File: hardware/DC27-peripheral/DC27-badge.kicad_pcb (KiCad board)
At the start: 2 copper layers, 106 parts, among them J1 Conn_01x02_Male, J2 USB_MICRO_RIGHT, J3 AudioJack3_Ground, J5 Conn_02x20_Odd_Even, J6 Conn_02x02_Counter_Clockwise, J7 Conn_ARM_JTAG_SWD_10, SW1 UP, SW2 DN, SW3 LEFT, SW4 RIGHT, SW5 A, SW6 B, SW7 RESET, U1 BMD-340-A-R, U2 IS31FL736, U3 MIC2288, U4 MCP73811T-435I-OT, U5 PAM2305AAB120, U6 MAX17043, U7 CS4344-CZZ, U8 TPD3E001DRLR

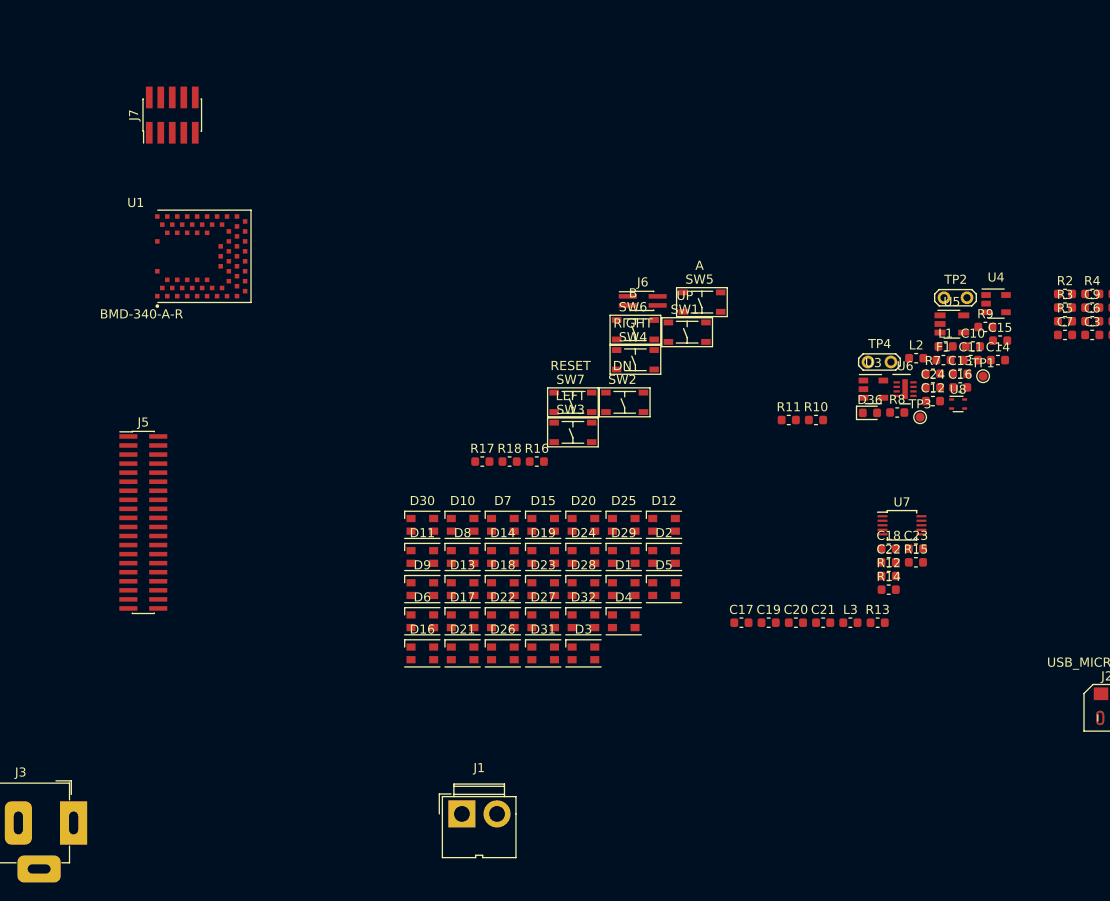
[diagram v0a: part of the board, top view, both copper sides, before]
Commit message: Update the main schematic with pins from bill's changes
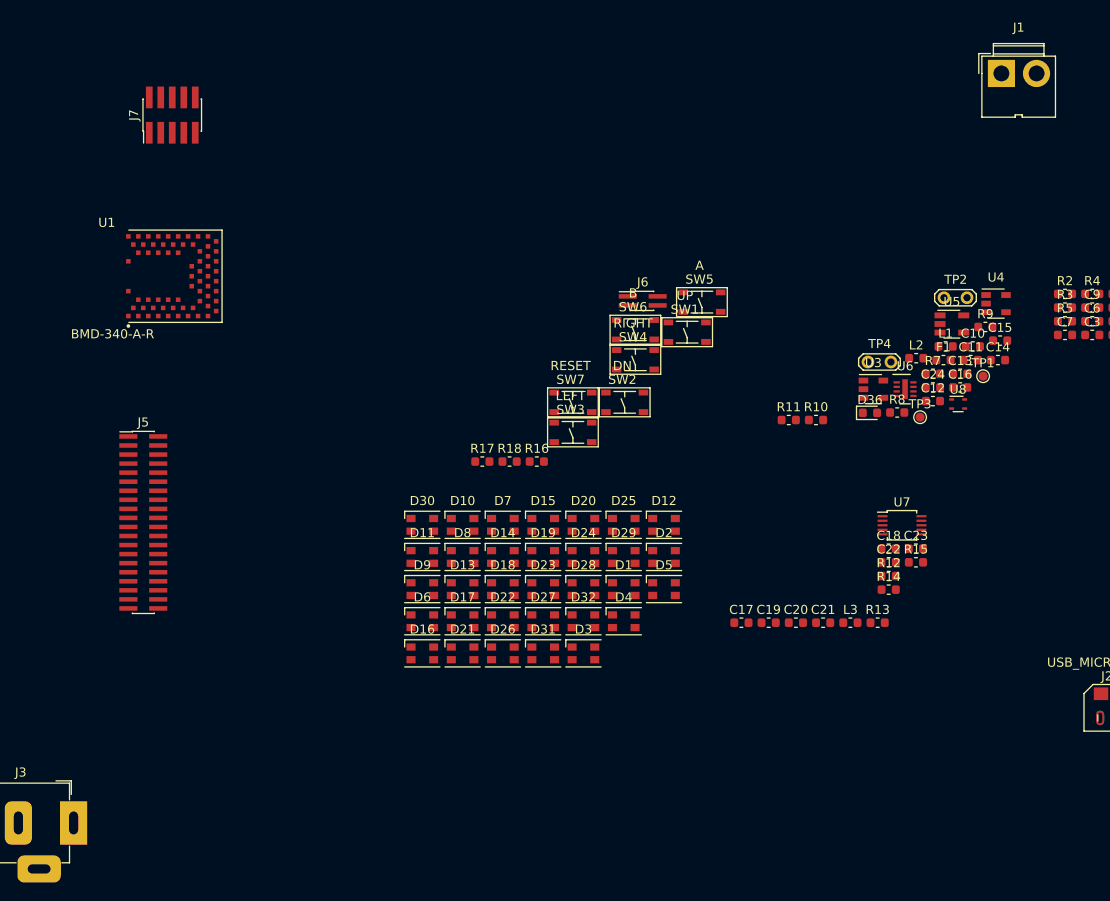
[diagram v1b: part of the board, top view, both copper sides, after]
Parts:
- moved J1 101.2 mm to (164.6, 30.8)
- moved U1 3.88 mm to (71.0, 53.2)
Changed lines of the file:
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@@
   )
   (module BMD-340-A-R:RIGADO_BMD-340-A-R (layer F.Cu)
-    (at 74.2 51)
+    (at 71 53.2)
     (attr smd)
     (fp_text reference U1 (at -5.23628 -5.9147) (layer F.SilkS)
@@
   )
   (module Connector:JWT_A3963_1x02_P3.96mm_Vertical (layer F.Cu)
-    (at 105 112.6)
+    (at 164.6 30.8)
     (descr "JWT A3963, 3.96mm pitch Pin head connector (http://www.jwt.com.tw/pro_pdf/A3963.pdf)")
     (tags "connector JWT A3963 pinhead")

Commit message: checkpoint everything - schematic passing DRC
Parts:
- removed C1, C3, C5, C7: 0.47uF, Capacitor_SMD:C_0603_1608Metric
- removed C10, C12, C13: 4.7uF, Capacitor_SMD:C_0603_1608Metric
- removed C11, C15: 22uF, Capacitor_SMD:C_0603_1608Metric
- removed C14, C23: 10uF, Capacitor_SMD:C_0603_1608Metric
- removed C16: 1.0uF, Capacitor_SMD:C_0603_1608Metric
- removed C17, C18, C19, C2, C24, C4, C6, C8: 0.1uF, Capacitor_SMD:C_0603_1608Metric
- removed C20, C21, C22: 3.3uF, Capacitor_SMD:C_0603_1608Metric
- removed C9: C, Capacitor_SMD:C_0603_1608Metric
- removed D1, D10, D11, D12, D13, D14, D15, D16, D17, D18, D19, D2, D20, D21, D22, D23, D24, D25, D26, D27, D28, D29, D3, D30, D31, D32, D4, D5, D6, D7, D8, D9: LED_ARGB, LED_SMD:LED_Cree-PLCC4_3.2x2.8mm_CCW
- removed D33, D35: MBRA140, Diode_SMD:D_SMA
- removed D36: LED, LED_SMD:LED_0603_1608Metric
- removed F1: 1.1A, Fuse:Fuse_0603_1608Metric
- removed J1: Conn_01x02_Male, Connector:JWT_A3963_1x02_P3.96mm_Vertical
- removed J2: USB_MICRO_RIGHT, MF_Connectors:MF_Connectors-MICROUSB-RIGHT
- removed J3: AudioJack3_Ground, Connector_Audio:Jack_Horizontal
- removed J5: Conn_02x20_Odd_Even, Connector_PinHeader_1.00mm:PinHeader_2x20_P1.00mm_Vertical_SMD
- removed J6: Conn_02x02_Counter_Clockwise, Connector_PinHeader_1.00mm:PinHeader_2x02_P1.00mm_Vertical_SMD
- removed J7: Conn_ARM_JTAG_SWD_10, Connector_PinHeader_1.27mm:PinHeader_2x05_P1.27mm_Vertical_SMD
- removed L1, L2: 4.7uH, Inductor_SMD:L_0603_1608Metric
- removed L3: L_Core_Ferrite, Inductor_SMD:L_0603_1608Metric
- removed R1, R4, R6: 100k, Resistor_SMD:R_0603_1608Metric
- removed R10: 2.0k, Resistor_SMD:R_0603_1608Metric
- removed R11, R2, R3: 1k, Resistor_SMD:R_0603_1608Metric
- removed R12, R13: 470, Resistor_SMD:R_0603_1608Metric
- removed R14, R15, R16: 10K, Resistor_SMD:R_0603_1608Metric
- removed R17, R18: 27k, Resistor_SMD:R_0603_1608Metric
- removed R5: 20K, Resistor_SMD:R_0603_1608Metric
- removed R7: 5k62, Resistor_SMD:R_0603_1608Metric
- removed R8: 1k87, Resistor_SMD:R_0603_1608Metric
- removed R9: 330, Resistor_SMD:R_0603_1608Metric
- removed SW1: UP, MF_Switches:MF_Switches-TACT4.2MM
- removed SW2: DN, MF_Switches:MF_Switches-TACT4.2MM
- removed SW3: LEFT, MF_Switches:MF_Switches-TACT4.2MM
- removed SW4: RIGHT, MF_Switches:MF_Switches-TACT4.2MM
- removed SW5: A, MF_Switches:MF_Switches-TACT4.2MM
- removed SW6: B, MF_Switches:MF_Switches-TACT4.2MM
- removed SW7: RESET, MF_Switches:MF_Switches-TACT4.2MM
- removed TP1: VIN, TestPoint:TestPoint_Pad_D1.0mm
- removed TP2: 5v TEST, TestPoint:TestPoint_2Pads_Pitch2.54mm_Drill0.8mm
- removed TP3: VBATT, TestPoint:TestPoint_Pad_D1.0mm
- removed TP4: 3.3V TEST, TestPoint:TestPoint_2Pads_Pitch2.54mm_Drill0.8mm
- removed U1: BMD-340-A-R, BMD-340-A-R:RIGADO_BMD-340-A-R
- removed U2: IS31FL736, dc27-sao-extras:QFN-40-1EP_5x5mm_P0.4mm_EP3.5x3.5mm
- removed U3: MIC2288, Package_TO_SOT_SMD:SOT-23-5
- removed U4: MCP73811T-435I-OT, Package_TO_SOT_SMD:SOT-23-5
- removed U5: PAM2305AAB120, Package_TO_SOT_SMD:TSOT-23-5
- removed U6: MAX17043, Package_DFN_QFN:DFN-8-1EP_2x3mm_P0.5mm_EP0.61x2.2mm
- removed U7: CS4344-CZZ, Housings_SSOP:TSSOP-10_3x3mm_Pitch0.5mm
- removed U8: TPD3E001DRLR, Package_TO_SOT_SMD:SOT-543
- added BT401: Battery, Connector_JST:JST_PH_S2B-PH-SM4-TB_1x02-1MP_P2.00mm_Horizontal, B.Cu at (105.0, 130.0)
- added C101: 12pF, Capacitor_SMD:C_0805_2012Metric, F.Cu at (40.8, -27.0)
- added C102: 12pF, Capacitor_SMD:C_0805_2012Metric, F.Cu at (27.7, -12.6)
- added C301: 1uF, Capacitor_SMD:C_0603_1608Metric, F.Cu at (85.4, -21.2)
- added C302: 0.1uF, Capacitor_SMD:C_0603_1608Metric, F.Cu at (85.7, -24.2)
- added C303: 1uF, Capacitor_SMD:C_0603_1608Metric, F.Cu at (85.7, -25.7)
- added C304: 0.1uF, Capacitor_SMD:C_0603_1608Metric, F.Cu at (82.7, -24.2)
- added C305: 1uF, Capacitor_SMD:C_0603_1608Metric, F.Cu at (82.7, -25.7)
- added C306: 0.1uF, Capacitor_SMD:C_0603_1608Metric, F.Cu at (79.4, -20.9)
- added C307: 1uF, Capacitor_SMD:C_0603_1608Metric, F.Cu at (82.7, -27.2)
- added C308: 0.1uF, Capacitor_SMD:C_0603_1608Metric, F.Cu at (76.4, -20.9)
- added C309: 1uF, Capacitor_SMD:C_0603_1608Metric, F.Cu at (82.7, -22.7)
- added C401: 10uF, Capacitor_SMD:C_1206_3216Metric, F.Cu at (64.4, -26.8)
- added C402: 10uF, Capacitor_SMD:C_1206_3216Metric, F.Cu at (62.1, -21.3)
- added C403: 10uF, Capacitor_SMD:C_1206_3216Metric, F.Cu at (57.5, -16.7)
- added C404: 10uF, Capacitor_SMD:C_1206_3216Metric, F.Cu at (64.4, -24.5)
- added C405: 10uF, Capacitor_SMD:C_1206_3216Metric, F.Cu at (57.5, -19.0)
- added C406: 1uF, Capacitor_SMD:C_1206_3216Metric, F.Cu at (57.5, -21.3)
- added C407: 1.0uF, Capacitor_SMD:C_0603_1608Metric, F.Cu at (64.3, -14.9)
- added C501: 0.1uF, Capacitor_SMD:C_0603_1608Metric, F.Cu at (92.1, 28.1)
- added C502: 1mF, Capacitor_SMD:C_0603_1608Metric, F.Cu at (103.0, 17.2)
- added C503: 0.1uF, Capacitor_SMD:C_0603_1608Metric, F.Cu at (101.4, 21.1)
- added C504: 3.3uF, Capacitor_SMD:C_0603_1608Metric, F.Cu at (98.5, 24.8)
- added C505: 100uF, Capacitor_SMD:C_0603_1608Metric, F.Cu at (95.1, 28.1)
- added C506: 3.3uF, Capacitor_SMD:C_0603_1608Metric, F.Cu at (101.4, 22.6)
- added C507: 0.1uF, Capacitor_SMD:C_0603_1608Metric, F.Cu at (95.4, 24.8)
- added C508: 3.3uF, Capacitor_SMD:C_0603_1608Metric, F.Cu at (89.1, 28.1)
- added C509: 10uF, Capacitor_SMD:C_0603_1608Metric, F.Cu at (103.0, 15.7)
- added C510: 100uF, Capacitor_SMD:C_0603_1608Metric, F.Cu at (86.1, 28.1)
- added C511: 1uF Ceramic, Capacitor_SMD:C_0603_1608Metric, F.Cu at (83.0, 28.1)
- added C601: 10uF, Capacitor_SMD:C_1206_3216Metric, F.Cu at (146.7, 37.0)
- added C602: 0.1uF, Capacitor_SMD:C_0603_1608Metric, F.Cu at (148.9, 38.9)
- added C603: 10uF, Capacitor_SMD:C_1206_3216Metric, F.Cu at (141.7, 42.3)
- added C604: 0.1uF, Capacitor_SMD:C_0603_1608Metric, F.Cu at (145.9, 40.5)
- added D201: LED_ARGB, LED_SMD:LED_Cree-PLCC4_3.2x2.8mm_CCW, F.Cu at (277.8, 73.8)
- added D202: LED_ARGB, LED_SMD:LED_Cree-PLCC4_3.2x2.8mm_CCW, F.Cu at (282.2, 70.2)
- added D203: LED_ARGB, LED_SMD:LED_Cree-PLCC4_3.2x2.8mm_CCW, F.Cu at (268.9, 84.4)
- added D204: LED_ARGB, LED_SMD:LED_Cree-PLCC4_3.2x2.8mm_CCW, F.Cu at (277.8, 80.9)
- added D205: LED_ARGB, LED_SMD:LED_Cree-PLCC4_3.2x2.8mm_CCW, F.Cu at (273.3, 84.4)
- added D206: LED_ARGB, LED_SMD:LED_Cree-PLCC4_3.2x2.8mm_CCW, F.Cu at (282.2, 73.8)
- added D207: LED_ARGB, LED_SMD:LED_Cree-PLCC4_3.2x2.8mm_CCW, F.Cu at (277.8, 77.3)
- added D208: LED_ARGB, LED_SMD:LED_Cree-PLCC4_3.2x2.8mm_CCW, F.Cu at (273.3, 77.3)
- added D209: LED_ARGB, LED_SMD:LED_Cree-PLCC4_3.2x2.8mm_CCW, F.Cu at (282.2, 77.3)
- added D210: LED_ARGB, LED_SMD:LED_Cree-PLCC4_3.2x2.8mm_CCW, F.Cu at (277.8, 70.2)
- added D211: LED_ARGB, LED_SMD:LED_Cree-PLCC4_3.2x2.8mm_CCW, F.Cu at (254.0, 62.0)
- added D212: LED_ARGB, LED_SMD:LED_Cree-PLCC4_3.2x2.8mm_CCW, F.Cu at (260.0, 62.0)
- added D213: LED_ARGB, LED_SMD:LED_Cree-PLCC4_3.2x2.8mm_CCW, F.Cu at (260.0, 70.2)
- added D214: LED_ARGB, LED_SMD:LED_Cree-PLCC4_3.2x2.8mm_CCW, F.Cu at (255.5, 77.3)
- added D215: LED_ARGB, LED_SMD:LED_Cree-PLCC4_3.2x2.8mm_CCW, F.Cu at (260.0, 73.8)
- added D216: LED_ARGB, LED_SMD:LED_Cree-PLCC4_3.2x2.8mm_CCW, F.Cu at (264.4, 70.2)
- added D217: LED_ARGB, LED_SMD:LED_Cree-PLCC4_3.2x2.8mm_CCW, F.Cu at (255.5, 80.9)
- added D218: LED_ARGB, LED_SMD:LED_Cree-PLCC4_3.2x2.8mm_CCW, F.Cu at (260.0, 77.3)
- added D219: LED_ARGB, LED_SMD:LED_Cree-PLCC4_3.2x2.8mm_CCW, F.Cu at (264.4, 73.8)
- added D220: LED_ARGB, LED_SMD:LED_Cree-PLCC4_3.2x2.8mm_CCW, F.Cu at (268.9, 70.2)
- added D221: LED_ARGB, LED_SMD:LED_Cree-PLCC4_3.2x2.8mm_CCW, F.Cu at (255.5, 84.4)
- added D222: LED_ARGB, LED_SMD:LED_Cree-PLCC4_3.2x2.8mm_CCW, F.Cu at (260.0, 80.9)
- added D223: LED_ARGB, LED_SMD:LED_Cree-PLCC4_3.2x2.8mm_CCW, F.Cu at (264.4, 77.3)
- added D224: LED_ARGB, LED_SMD:LED_Cree-PLCC4_3.2x2.8mm_CCW, F.Cu at (268.9, 73.8)
- added D225: LED_ARGB, LED_SMD:LED_Cree-PLCC4_3.2x2.8mm_CCW, F.Cu at (273.3, 70.2)
- added D226: LED_ARGB, LED_SMD:LED_Cree-PLCC4_3.2x2.8mm_CCW, F.Cu at (260.0, 84.4)
- added D227: LED_ARGB, LED_SMD:LED_Cree-PLCC4_3.2x2.8mm_CCW, F.Cu at (264.4, 80.9)
- added D228: LED_ARGB, LED_SMD:LED_Cree-PLCC4_3.2x2.8mm_CCW, F.Cu at (268.9, 77.3)
- added D229: LED_ARGB, LED_SMD:LED_Cree-PLCC4_3.2x2.8mm_CCW, F.Cu at (273.3, 73.8)
- added D230: LED_ARGB, LED_SMD:LED_Cree-PLCC4_3.2x2.8mm_CCW, F.Cu at (273.3, 80.9)
- added D231: LED_ARGB, LED_SMD:LED_Cree-PLCC4_3.2x2.8mm_CCW, F.Cu at (264.4, 84.4)
- added D232: LED_ARGB, LED_SMD:LED_Cree-PLCC4_3.2x2.8mm_CCW, F.Cu at (268.9, 80.9)
- added D401: CHG, Diode_SMD:D_0603_1608Metric, F.Cu at (65.9, -22.6)
- added D402: DONE, Diode_SMD:D_0603_1608Metric, F.Cu at (56.7, -14.8)
- added D601: TX LED, Diode_SMD:D_0603_1608Metric, F.Cu at (145.9, 38.9)
- added D602: RX LED, Diode_SMD:D_0603_1608Metric, F.Cu at (150.5, 36.6)
- added J101: Conn_ARM_JTAG_SWD_10, Connector_PinHeader_1.27mm:PinHeader_2x05_P1.27mm_Vertical_SMD, F.Cu at (34.0, -20.3)
- added J102: ShittyAddOnL, Connector_PinSocket_2.54mm:PinSocket_2x02_P2.54mm_Vertical_SMD, F.Cu at (29.1, -52.0)
- added J103: ShittyAddOnR, Connector_PinSocket_2.54mm:PinSocket_2x02_P2.54mm_Vertical_SMD, F.Cu at (213.8, 76.1)
- added J104: Conn_02x20_Odd_Even, Connector_PinSocket_2.54mm:PinSocket_2x20_P2.54mm_Vertical_SMD, F.Cu at (104.5, 95.0)
- added J105: Conn_01x02_Female, Connector_PinHeader_1.00mm:PinHeader_1x02_P1.00mm_Horizontal, F.Cu at (30.8, -234.5)
- added J501: SPK LEFT, Connector_PinSocket_2.54mm:PinSocket_1x02_P2.54mm_Vertical_SMD_Pin1Left, F.Cu at (83.0, 72.0)
- added J502: SPK_RIGHT, Connector_PinSocket_2.54mm:PinSocket_1x02_P2.54mm_Vertical_SMD_Pin1Left, F.Cu at (213.9, 64.3)
- added J601: USB_MICRO_RIGHT, MF_Connectors:MF_Connectors-MICROUSB-RIGHT, F.Cu at (139.3, 38.2)
- added L601: LXES15AAA1-153, Diode_SMD:D_01005_0402Metric, F.Cu at (144.8, 43.1)
- added L602: LXES15AAA1-153, Diode_SMD:D_01005_0402Metric, F.Cu at (152.9, 36.2)
- added L603: LXES15AAA1-153, Diode_SMD:D_01005_0402Metric, F.Cu at (149.9, 37.8)
- added MH701: DISP UL, MountingHole:MountingHole_3.2mm_M3_DIN965, F.Cu at (209.5, 32.2)
- added MH702: DISP UR, MountingHole:MountingHole_3.2mm_M3_DIN965, F.Cu at (230.6, 32.1)
- added MH703: DISP LL, MountingHole:MountingHole_3.2mm_M3_DIN965, F.Cu at (209.7, 43.5)
- added MH704: DISP LR, MountingHole:MountingHole_3.2mm_M3_DIN965, F.Cu at (230.3, 44.1)
- added MH705: LANYARD1, MountingHole:MountingHole_3.2mm_M3_DIN965, F.Cu at (186.7, 32.3)
- added MH706: LANYARD2, MountingHole:MountingHole_3.2mm_M3_DIN965, F.Cu at (195.6, 32.3)
- added R101: 10K, Resistor_SMD:R_0603_1608Metric, F.Cu at (28.7, -17.7)
- added R301: 10k, Resistor_SMD:R_0603_1608Metric, F.Cu at (85.7, -22.7)
- added R302: 20K, Resistor_SMD:R_0603_1608Metric, F.Cu at (85.7, -27.2)
- added R303: 10k, Resistor_SMD:R_0603_1608Metric, F.Cu at (82.4, -20.9)
- added R401: R, Resistor_SMD:R_0603_1608Metric, F.Cu at (61.3, -15.7)
- added R402: R, Resistor_SMD:R_0603_1608Metric, F.Cu at (67.5, -16.5)
- added R403: 2.0k, Resistor_SMD:R_0603_1608Metric, F.Cu at (67.5, -18.0)
- added R404: 1k, Resistor_SMD:R_0603_1608Metric, F.Cu at (68.9, -20.5)
- added R501: 20K, Resistor_SMD:R_0603_1608Metric, F.Cu at (98.5, 26.3)
- added R502: 20K, Resistor_SMD:R_0603_1608Metric, F.Cu at (104.4, 20.2)
- added R503: 20K, Resistor_SMD:R_0603_1608Metric, F.Cu at (95.4, 26.3)
- added R504: 20K, Resistor_SMD:R_0603_1608Metric, F.Cu at (103.0, 18.7)
- added R601: 1k, Resistor_SMD:R_0603_1608Metric, F.Cu at (143.9, 44.2)
- added R602: 47, Resistor_SMD:R_0603_1608Metric, F.Cu at (143.9, 45.7)
- added R603: 47, Resistor_SMD:R_0603_1608Metric, F.Cu at (140.9, 45.7)
- added R604: 22.1k, Resistor_SMD:R_0603_1608Metric, F.Cu at (140.9, 44.2)
- added R605: 47.5k, Resistor_SMD:R_0603_1608Metric, F.Cu at (145.5, 42.0)
- added SW101: UP, MF_Switches:MF_Switches-TACT4.2MM, F.Cu at (26.3, -8.60)
- added SW102: DN, MF_Switches:MF_Switches-TACT4.2MM, F.Cu at (36.3, -23.0)
- added SW103: LEFT, MF_Switches:MF_Switches-TACT4.2MM, F.Cu at (28.9, -15.2)
- added SW104: RIGHT, MF_Switches:MF_Switches-TACT4.2MM, F.Cu at (23.2, -11.9)
- added SW105: A, MF_Switches:MF_Switches-TACT4.2MM, F.Cu at (20.6, -7.79)
- added SW106: B, MF_Switches:MF_Switches-TACT4.2MM, F.Cu at (23.2, -15.2)
- added SW107: ENTER, MF_Switches:MF_Switches-TACT4.2MM, F.Cu at (36.3, -26.3)
- added SW108: RESET, MF_Switches:MF_Switches-TACT4.2MM, F.Cu at (30.1, -20.1)
- added SW401: POWER ON, Button_Switch_SMD:SW_SPDT_PCM12, F.Cu at (50.7, -25.5)
- added TP101: SDT_SPI_MOSI, TestPoint:TestPoint_Pad_D2.0mm, F.Cu at (33.3, -16.8)
- added TP102: SDT_SPI_MISO, TestPoint:TestPoint_Pad_D2.0mm, F.Cu at (40.7, -24.5)
- added TP103: SDT_SPI_SCK, TestPoint:TestPoint_Pad_D2.0mm, F.Cu at (40.7, -21.4)
- added TP104: SDT_SPI_SCK, TestPoint:TestPoint_Pad_D2.0mm, F.Cu at (31.0, -12.1)
- added TP105: DISP_MOSI, TestPoint:TestPoint_Pad_D2.0mm, F.Cu at (30.7, -9.00)
- added TP106: DISP_MOSI, TestPoint:TestPoint_Pad_D2.0mm, F.Cu at (36.3, -16.8)
- added TP107: XTAL0, TestPoint:TestPoint_Pad_D2.0mm, F.Cu at (39.4, -18.4)
- added TP108: XTAL1, TestPoint:TestPoint_Pad_D2.0mm, F.Cu at (34.0, -13.7)
- added TP401: VBATT, TestPoint:TestPoint_Pad_D2.0mm, F.Cu at (64.4, -17.2)
- added TP402: 3.3V TEST, TestPoint:TestPoint_Pad_D2.0mm, F.Cu at (68.9, -22.8)
- added TP403: GND, TestPoint:TestPoint_Pad_D2.0mm, F.Cu at (65.9, -20.3)
- added U101: BMD-340-A-R, BMD-340-A-R:RIGADO_BMD-340-A-R, F.Cu at (21.7, -35.5)
- added U301: IS31FL3216A, Package_DFN_QFN:QFN-40-1EP_5x5mm_P0.4mm_EP3.6x3.6mm, F.Cu at (78.1, -24.8)
- added U401: MCP73831-2-OT, Package_TO_SOT_SMD:SOT-23-5, F.Cu at (68.6, -26.1)
- added U402: LM1117-3.3, Package_TO_SOT_SMD:SOT-223, F.Cu at (50.7, -18.4)
- added U403: MAX17043, Package_DFN_QFN:DFN-8-1EP_2x3mm_P0.5mm_EP0.61x2.2mm, F.Cu at (61.3, -18.3)
- added U501: CS4344-CZZ, Housings_SSOP:TSSOP-10_3x3mm_Pitch0.5mm, F.Cu at (96.9, 22.2)
- added U502: LM4880, Package_SO:SOIC-8_3.9x4.9mm_P1.27mm, F.Cu at (97.7, 17.6)
- added U601: CP2102N-A01-GQFN28, Package_DFN_QFN:QFN-28-1EP_5x5mm_P0.5mm_EP3.35x3.35mm_ThermalVias, F.Cu at (136.7, 43.8)
- added Y101: 32.768Khz XTAL, Crystal:Crystal_SMD_MicroCrystal_CC4V-T1A-2Pin_5.0x1.9mm, F.Cu at (14.7, -8.02)

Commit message: try to clean up the schematic and libraries
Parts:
- J104: footprint Connector_PinSocket_2.54mm:PinSocket_2x20_P2.54mm_Vertical_SMD -> jna-parts:SAMTEC-SSM-120-X-DV
- moved J105 408.3 mm to (253.0, 108.0)
- moved C101 292.4 mm to (277.3, 145.0)
- moved C401 292.4 mm to (300.9, 145.2)
- moved C404 292.4 mm to (300.9, 147.5)
- moved R101 292.4 mm to (265.2, 154.3)
- moved SW104 292.4 mm to (259.7, 160.1)
- moved SW106 292.4 mm to (259.7, 156.8)
- moved SW401 292.4 mm to (287.2, 146.5)
- moved TP101 292.4 mm to (269.8, 155.2)
- moved TP102 292.4 mm to (277.2, 147.5)
- moved TP103 292.4 mm to (277.2, 150.6)
- moved TP104 292.4 mm to (267.5, 159.9)
- moved U402 292.4 mm to (287.2, 153.6)
- moved C102 292.4 mm to (264.2, 159.4)
- moved C308 292.4 mm to (312.9, 151.1)
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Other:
- board outline added: 140 x 80 mm
- board text added: "SCREEN MODULE OUTLINE"
